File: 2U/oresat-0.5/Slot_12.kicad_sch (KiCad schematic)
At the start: 2 parts

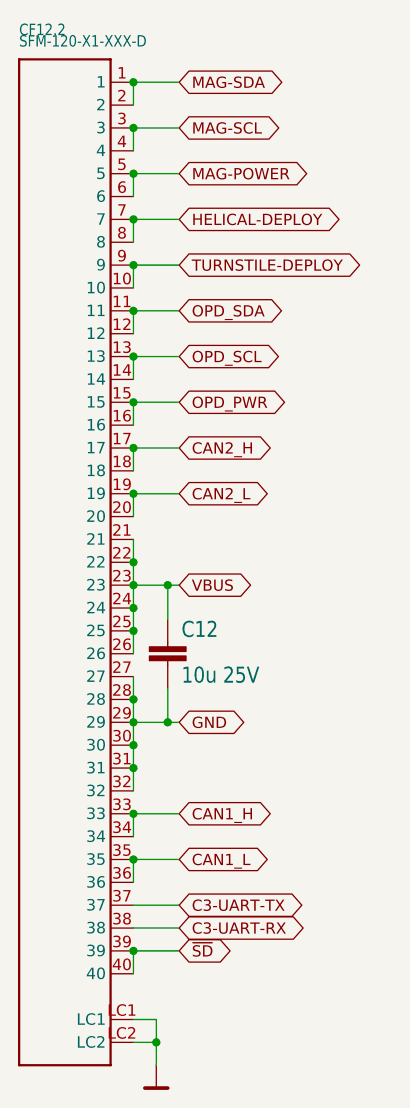
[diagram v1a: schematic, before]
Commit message: Fixed all (most) of the issues from Eagle imports
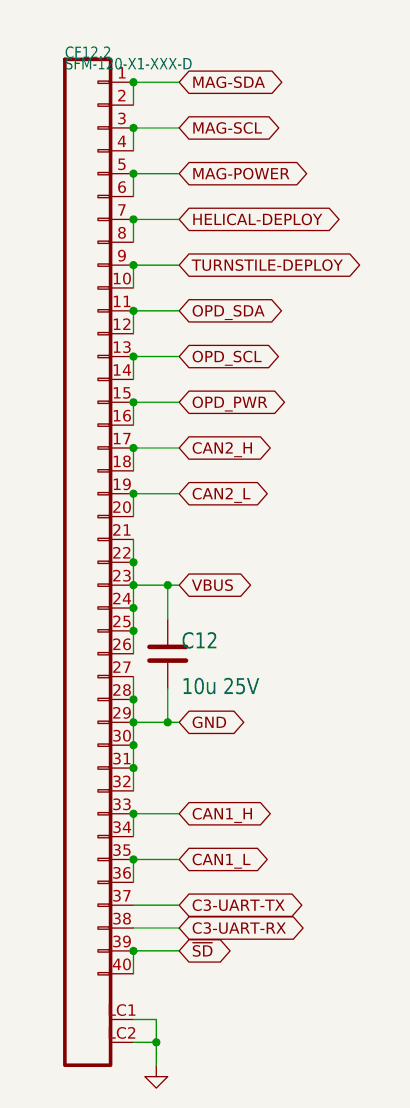
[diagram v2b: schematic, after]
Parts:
- C12: symbol oresat0-1u-backplane-eagle-import:C-EU1206-B -> Device:C
- CF12.2: symbol oresat-backplane-2u-eagle-import:SFM-120-X1-XXX-D -> oresat-connectors:J-SAMTEC-TFM-120-01-L-D-RA

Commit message: Moved entire schematic to single page
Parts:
- removed C12: 10u 25V, Capacitor_SMD:C_1206_3216Metric, symbol Device:C
- removed CF12.2: SFM-120-X1-XXX-D, oresat-connectors:J-SAMTEC-SFM-120-X1-XXX-D, symbol oresat-connectors:J-SAMTEC-TFM-120-01-L-D-RA
